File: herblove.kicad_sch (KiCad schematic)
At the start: 6 parts, among them J1 Micro_SD_Card, SW1 SW_Push, SW2 SW_SPDT, U1 bme280, U2 C3 Pico, U3 hw357

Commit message: Add final components
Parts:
- removed J1: Micro_SD_Card, sd-card:sd-card, symbol Connector:Micro_SD_Card
- added BT1: Battery_Cell, Connector_JST:JST_PH_B2B-PH-K_1x02_P2.00mm_Vertical, symbol Device:Battery_Cell
- added J2: 12V Valve, Connector_PinHeader_2.54mm:PinHeader_1x02_P2.54mm_Vertical, symbol Connector:Conn_01x02_Pin
- added J3: Empty Sensor, Connector_PinHeader_2.54mm:PinHeader_1x02_P2.54mm_Vertical, symbol Connector:Conn_01x02_Pin
- added J4: Switched Battery, Connector_JST:JST_PH_B2B-PH-K_1x02_P2.00mm_Vertical, symbol Connector:Conn_01x02_Pin
- added J5: Solar Panel, Connector_JST:JST_PH_B2B-PH-K_1x02_P2.00mm_Vertical, symbol Connector:Conn_01x02_Pin
- added J6: Micro_SD_Card, sd-card:sd-card, symbol Connector:Micro_SD_Card
- added SW3: SW_Push, pts636:pts636, symbol Switch:SW_Push
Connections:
- net SWITCH_A: now reaches SW1.1
- net GND: now reaches SW1.2
- net GND: now also U2.2 (GND), U3.2 (IN-), J2.1 (Pin_1), J3.1 (Pin_1), J4.1 (Pin_1), J5.1 (Pin_1), J6.6 (VSS), J6.9 (SHIELD), SW3.2
- net at U3.1 (IN+): now also J5.2 (Pin_2)
- net +12V: now reaches U3.3 (O+)
- net +12V: now also J2.2 (Pin_2)
- net at U3.5 (B+): now also SW2.1 (A), BT1.1 (+)
- net at U3.6 (B-): now also BT1.2 (-)
- net at SW2.2 (B): now also J4.2 (Pin_2)
- net +3V3: now reaches U1.1 (VIN)
- net +3V3: now also U2.9 (3V3), J6.4 (VDD)
- net SCL: now reaches U1.3 (SCL)
- net SCL: now also U2.6 (SCL/IO10)
- net SDA: now reaches U1.4 (SDA)
- net SDA: now also U2.5 (SDA/IO8)
- new net EMPTY_SENSOR: J3.2 (Pin_2)
- new net SPI_CLK: J6.5 (CLK)
- new net SPI_CS: J6.2 (DAT3/CD)
- new net SPI_MISO: J6.7 (DAT0)
- new net SPI_MOSI: J6.3 (CMD)
- new net SWITCH_B: SW3.1
- no-connect marks 0 -> 9
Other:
- moved on the sheet: SW2, U2

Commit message: Finalise routing
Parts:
- added J1: Conn_01x01_Pin, Connector_PinHeader_2.54mm:PinHeader_1x01_P2.54mm_Vertical, symbol Connector:Conn_01x01_Pin
- added J7: Conn_01x04_Pin, Connector_PinHeader_2.54mm:PinHeader_1x04_P2.54mm_Vertical, symbol Connector:Conn_01x04_Pin
- added R1, R2, R3, R4: 1k, Resistor_THT:R_Axial_DIN0207_L6.3mm_D2.5mm_P7.62mm_Horizontal, symbol Device:R_Small
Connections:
- net +3V3: now also J7.2 (Pin_2), R4.1
- net EMPTY_SENSOR: now also R1.2, R2.1
- net ENABLE_12V: now also U2.14 (IO2), J1.1 (Pin_1)
- net GND: now also U1.2 (GND), J7.1 (Pin_1)
- net SCL: now also J7.4 (Pin_4)
- net SDA: now also J7.3 (Pin_3)
- net SPI_CLK: now also U2.12 (IO0/ADC/MISO)
- net SPI_CS: now also U2.10 (IO5)
- net SPI_MISO: now also U2.13 (IO1/ADC/SCK)
- net SPI_MOSI: now also U2.11 (IO4/MOSI)
- net SWITCH_A: now also R3.2
- net SWITCH_B: now also R2.2, R3.1
- net BUTTONS_ADC: now reaches U2.3 (IO6)
- net BUTTONS_ADC: now also R1.1, R4.2

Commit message: Ground all the negative terminals of the battery step up converter
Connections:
- net GND: now also BT1.2 (-), U3.4 (O-), U3.6 (B-)
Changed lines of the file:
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@@
 	(paper "A4")
+	(junction
+		(at 119.38 45.72)
+		(diameter 0)
+		(color 0 0 0 0)
+	)
 	(junction
 		(at 114.3 38.1)
@@
 				(path "/aea06310-3436-46a1-8b8b-19bfbdf98433"
 					(reference "#PWR013")
+					(unit 1)
+				)
+			)
+		)
+	)
+	(symbol
+		(lib_id "power:GND")
+		(at 134.62 45.72 0)
+		(unit 1)
+		(exclude_from_sim no)
+		(in_bom yes)
+		(on_board yes)
+		(dnp no)
+		(fields_autoplaced yes)
+		(property "Reference" "#PWR019"
+			(at 134.62 52.07 0)
+			(effects
+				(font
+					(size 1.27 1.27)
+				)
+				(hide yes)
+			)
+		)
+		(property "Value" "GND"
+			(at 134.62 50.8 0)
+			(effects
+				(font
+					(size 1.27 1.27)
+				)
+			)
+		)
+		(property "Footprint" ""
+			(at 134.62 45.72 0)
+			(effects
+				(font
+					(size 1.27 1.27)
+				)
+				(hide yes)
+			)
+		)
+		(property "Datasheet" ""
+			(at 134.62 45.72 0)
+			(effects
+				(font
+					(size 1.27 1.27)
+				)
+				(hide yes)
+			)
+		)
+		(property "Description" "Power symbol creates a global label with name \"GND\" , ground"
+			(at 134.62 45.72 0)
+			(effects
+				(font
+					(size 1.27 1.27)
+				)
+				(hide yes)
+			)
+		)
+		(pin "1"
+		)
+		(instances
+			(project "herblove"
+				(path "/aea06310-3436-46a1-8b8b-19bfbdf98433"
+					(reference "#PWR019")
 					(unit 1)
 				)
@@
 					(unit 1)
 				)
+			)
+		)
+	)
+	(symbol
+		(lib_id "power:GND")
+		(at 119.38 45.72 0)
+		(unit 1)
+		(exclude_from_sim no)
+		(in_bom yes)
+		(on_board yes)
+		(dnp no)
+		(fields_autoplaced yes)
+		(property "Reference" "#PWR020"
+			(at 119.38 52.07 0)
+			(effects
+				(font
+					(size 1.27 1.27)
+				)
+				(hide yes)
+			)
+		)
+		(property "Value" "GND"
+			(at 119.38 50.8 0)
+			(effects
+				(font
+					(size 1.27 1.27)
+				)
+			)
+		)
+		(property "Footprint" ""
+			(at 119.38 45.72 0)
+			(effects
+				(font
+					(size 1.27 1.27)
+				)
+				(hide yes)
+			)
+		)
+		(property "Datasheet" ""
+			(at 119.38 45.72 0)
+			(effects
+				(font
+					(size 1.27 1.27)
+				)
+				(hide yes)
+			)
+		)
+		(property "Description" "Power symbol creates a global label with name \"GND\" , ground"
+			(at 119.38 45.72 0)
+			(effects
+				(font
+					(size 1.27 1.27)
+				)
+				(hide yes)
+			)
+		)
+		(pin "1"
+		)
+		(instances
+			(project "herblove"
+				(path "/aea06310-3436-46a1-8b8b-19bfbdf98433"
+					(reference "#PWR020")
+					(unit 1)
+				)

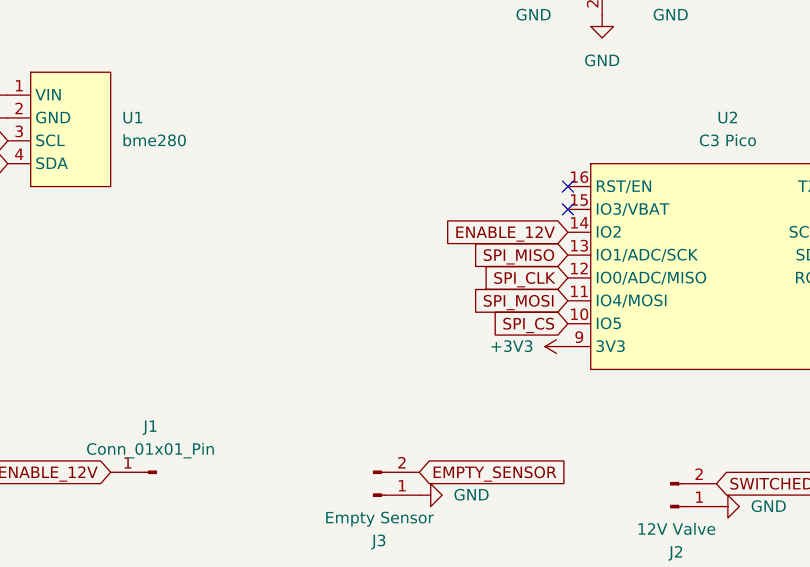
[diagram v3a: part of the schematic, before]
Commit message: Add a weak pull down for the enable pin of the step up converter
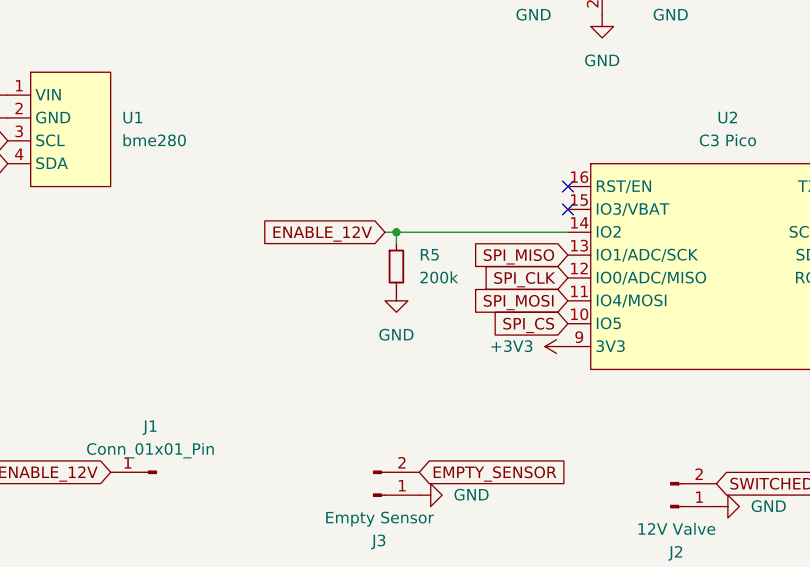
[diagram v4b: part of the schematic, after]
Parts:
- added R5: 200k, Resistor_THT:R_Axial_DIN0207_L6.3mm_D2.5mm_P7.62mm_Horizontal, symbol Device:R_Small
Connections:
- net ENABLE_12V: now also R5.1
- net GND: now also R5.2
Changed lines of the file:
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@@
+	)
+	(junction
+		(at 104.14 74.93)
+		(diameter 0)
+		(color 0 0 0 0)
 	)
 	(junction
@@
 	(wire
 		(pts
-			(xy 207.01 101.6) (xy 207.01 102.87)
+			(xy 104.14 74.93) (xy 123.19 74.93)
 		)
 		(stroke
@@
 	(wire
 		(pts
-			(xy 100.33 29.21) (xy 114.3 29.21)
+			(xy 207.01 101.6) (xy 207.01 102.87)
 		)
 		(stroke
@@
 	(wire
 		(pts
-			(xy 207.01 134.62) (xy 207.01 133.35)
+			(xy 100.33 29.21) (xy 114.3 29.21)
 		)
 		(stroke
@@
 	(wire
 		(pts
-			(xy 105.41 38.1) (xy 114.3 38.1)
+			(xy 207.01 134.62) (xy 207.01 133.35)
 		)
 		(stroke
@@
 	(wire
 		(pts
-			(xy 105.41 45.72) (xy 119.38 45.72)
+			(xy 105.41 38.1) (xy 114.3 38.1)
 		)
 		(stroke
@@
 	(wire
 		(pts
-			(xy 114.3 38.1) (xy 119.38 38.1)
+			(xy 105.41 45.72) (xy 119.38 45.72)
 		)
 		(stroke
@@
 	(wire
 		(pts
-			(xy 207.01 118.11) (xy 207.01 120.65)
+			(xy 114.3 38.1) (xy 119.38 38.1)
 		)
 		(stroke
@@
 	(wire
 		(pts
-			(xy 140.97 38.1) (xy 134.62 38.1)
+			(xy 104.14 76.2) (xy 104.14 74.93)
 		)
 		(stroke
@@
 		)
 	)
+	(wire
+		(pts
+			(xy 207.01 118.11) (xy 207.01 120.65)
+		)
+		(stroke
+			(width 0)
+			(type default)
+		)
+	)
+	(wire
+		(pts
+			(xy 102.87 74.93) (xy 104.14 74.93)
+		)
+		(stroke
+			(width 0)
+			(type default)
+		)
+	)
+	(wire
+		(pts
+			(xy 140.97 38.1) (xy 134.62 38.1)
+		)
+		(stroke
+			(width 0)
+			(type default)
+		)
+	)
 	(global_label "SWITCH_B"
 		(shape input)
@@
 	(global_label "ENABLE_12V"
 		(shape input)
-		(at 123.19 74.93 180)
+		(at 102.87 74.93 180)
 		(fields_autoplaced yes)
 		(effects
@@
 		)
 		(property "Intersheetrefs" "${INTERSHEET_REFS}"
-			(at 108.7144 74.93 0)
+			(at 88.3944 74.93 0)
 			(effects
 				(font
@@
 	(symbol
 		(lib_id "power:GND")
+		(at 104.14 81.28 0)
+		(mirror y)
+		(unit 1)
+		(exclude_from_sim no)
+		(in_bom yes)
+		(on_board yes)
+		(dnp no)
+		(fields_autoplaced yes)
+		(property "Reference" "#PWR021"
+			(at 104.14 87.63 0)
+			(effects
+				(font
+					(size 1.27 1.27)
+				)
+				(hide yes)
+			)
+		)
+		(property "Value" "GND"
+			(at 104.14 86.36 0)
+			(effects
+				(font
+					(size 1.27 1.27)
+				)
+			)
+		)
+		(property "Footprint" ""
+			(at 104.14 81.28 0)
+			(effects
+				(font
+					(size 1.27 1.27)
+				)
+				(hide yes)
+			)
+		)
+		(property "Datasheet" ""
+			(at 104.14 81.28 0)
+			(effects
+				(font
+					(size 1.27 1.27)
+				)
+				(hide yes)
+			)
+		)
+		(property "Description" "Power symbol creates a global label with name \"GND\" , ground"
+			(at 104.14 81.28 0)
+			(effects
+				(font
+					(size 1.27 1.27)
+				)
+				(hide yes)
+			)
+		)
+		(pin "1"
+		)
+		(instances
+			(project "herblove"
+				(path "/aea06310-3436-46a1-8b8b-19bfbdf98433"
+					(reference "#PWR021")
+					(unit 1)
+				)
+			)
+		)
+	)
+	(symbol
+		(lib_id "power:GND")
 		(at 127 50.8 0)
 		(unit 1)
@@
 					(unit 1)
 				)
+			)
+		)
+	)
+	(symbol
+		(lib_id "Device:R_Small")
+		(at 104.14 78.74 0)
+		(unit 1)
+		(exclude_from_sim no)
+		(in_bom yes)
+		(on_board yes)
+		(dnp no)
+		(fields_autoplaced yes)
+		(property "Reference" "R5"
+			(at 106.68 77.4699 0)
+			(effects
+				(font
+					(size 1.27 1.27)
+				)
+				(justify left)
+			)
+		)
+		(property "Value" "200k"
+			(at 106.68 80.0099 0)
+			(effects
+				(font
+					(size 1.27 1.27)
+				)
+				(justify left)
+			)
+		)
+		(property "Footprint" "Resistor_THT:R_Axial_DIN0207_L6.3mm_D2.5mm_P7.62mm_Horizontal"
+			(at 104.14 78.74 0)
+			(effects
+				(font
+					(size 1.27 1.27)
+				)
+				(hide yes)
+			)
+		)
+		(property "Datasheet" "~"
+			(at 104.14 78.74 0)
+			(effects
+				(font
+					(size 1.27 1.27)
+				)
+				(hide yes)
+			)
+		)
+		(property "Description" "Resistor, small symbol"
+			(at 104.14 78.74 0)
+			(effects
+				(font
+					(size 1.27 1.27)
+				)
+				(hide yes)
+			)
+		)
+		(pin "1"
+		)
+		(pin "2"
+		)
+		(instances
+			(project "herblove"
+				(path "/aea06310-3436-46a1-8b8b-19bfbdf98433"
+					(reference "R5")
+					(unit 1)
+				)

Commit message: Fix polarity of the solar plug
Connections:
- net GND: now also J5.2 (Pin_2); no longer J5.1 (Pin_1)
- net at U3.1 (IN+): now also J5.1 (Pin_1); no longer J5.2 (Pin_2)
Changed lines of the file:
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@@
 	(symbol
 		(lib_id "Connector:Conn_01x02_Pin")
-		(at 105.41 16.51 0)
-		(mirror x)
+		(at 105.41 13.97 0)
 		(unit 1)
 		(exclude_from_sim no)
@@
 		(dnp no)
 		(property "Reference" "J5"
-			(at 106.045 21.59 0)
+			(at 106.045 8.89 0)
 			(effects
 				(font
@@
 		)
 		(property "Value" "Solar Panel"
-			(at 106.045 19.05 0)
+			(at 106.045 11.43 0)
 			(effects
 				(font
@@
 		)
 		(property "Footprint" "Connector_JST:JST_PH_B2B-PH-K_1x02_P2.00mm_Vertical"
-			(at 105.41 16.51 0)
+			(at 105.41 13.97 0)
 			(effects
 				(font
@@
 		)
 		(property "Datasheet" "~"
-			(at 105.41 16.51 0)
+			(at 105.41 13.97 0)
 			(effects
 				(font
@@
 		)
 		(property "Description" "Generic connector, single row, 01x02, script generated"
-			(at 105.41 16.51 0)
+			(at 105.41 13.97 0)
 			(effects
 				(font
